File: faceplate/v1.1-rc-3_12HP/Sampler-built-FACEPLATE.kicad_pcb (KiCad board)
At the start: 4 copper layers, 60.6 x 128.5 mm, 24 parts

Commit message: created artwork assets for frontpanel, created and verified gerbers for front panel
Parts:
- removed SD1: microSDCon_Vert_TH_PJS008U-3000, 4ms_Connector_Card:CardSlot_MicroSD_YamaichiPJS008U-3000
- added ?: , , B.Cu at (22.8, 121.3)
- added G***: LOGO, artwork:Sampler-built-frontsilk-v1.1-rc-3_12hp, F.Cu at (23.0, 61.0)
- added REF**: Faceplate_SD_Card_Slot, 4ms_Faceplate:Faceplate_SD_Card_Slot, F.Cu at (22.7, 31.9)
- added REF**: Rail_Connection_12HP, 4ms_Faceplate:Rail_Connection_12HP, B.Cu at (22.8, 1.25)
- moved REF** 9.51 mm to (30.0, 108.7)
- moved REF** 9.51 mm to (30.0, 93.7)
- moved REF** 9.51 mm to (44.5, 93.7)
- moved REF** 9.51 mm to (0.00, 122.5)
- moved REF** 9.51 mm to (0.94, 108.7)
- moved REF** 9.51 mm to (15.5, 93.7)
- moved REF** 9.51 mm to (45.6, 122.5)
- moved REF** 9.51 mm to (0.94, 93.7)
- moved REF** 9.51 mm to (44.5, 108.7)
- moved REF** 9.51 mm to (15.5, 108.7)
- moved LOCK1 9.51 mm to (22.8, 14.4)
- moved REF** 9.51 mm to (41.1, 12.3)
- moved REF** 9.51 mm to (4.13, 27.0)
- moved REF** 9.51 mm to (41.1, 53.0)
- moved REF** 9.51 mm to (4.13, 53.0)
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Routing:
- removed copper zone on In2.Cu, net +3V3
- removed copper zone on In1.Cu, net GND

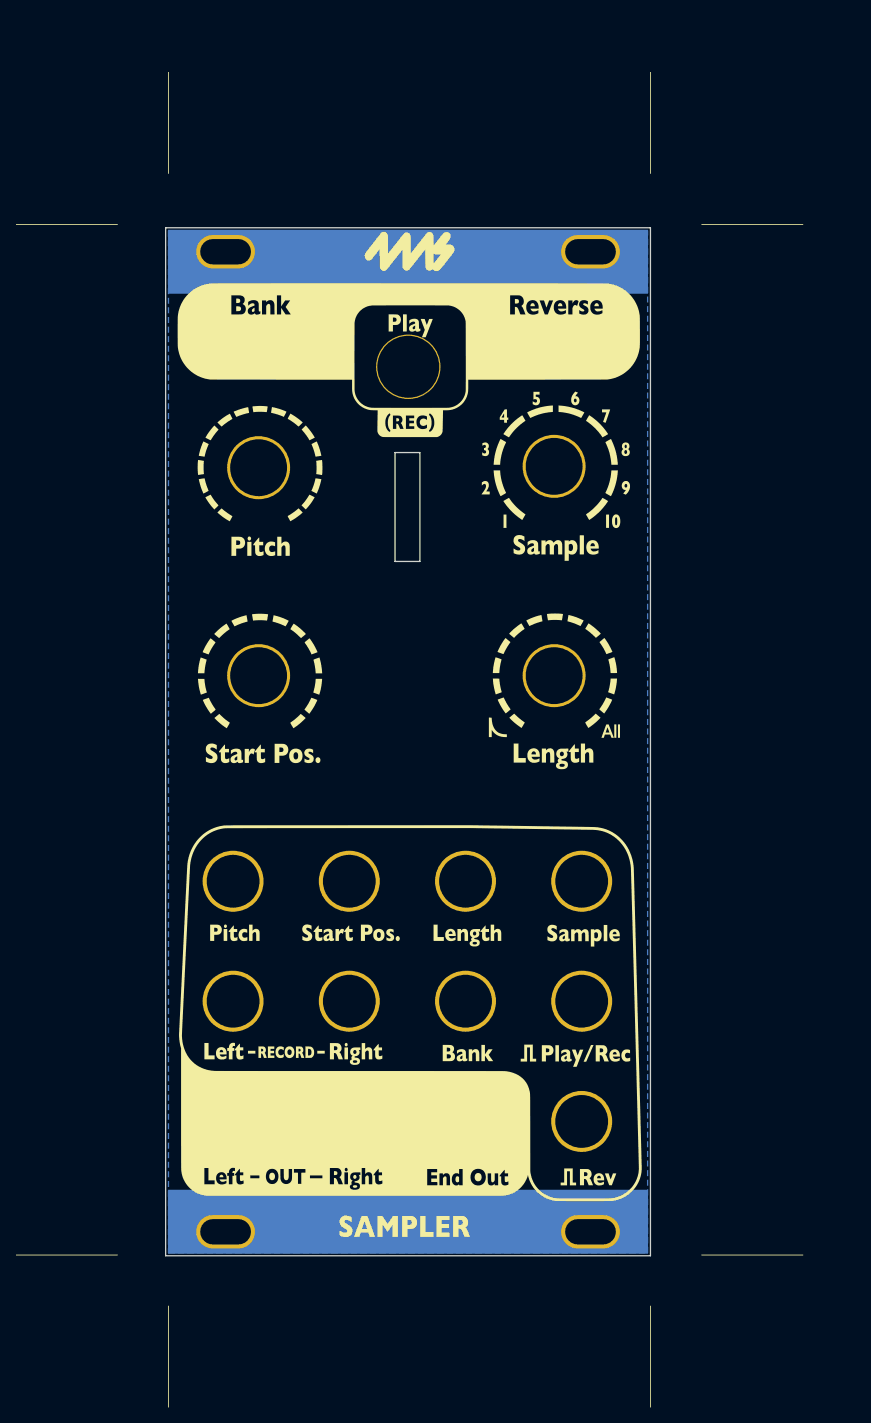
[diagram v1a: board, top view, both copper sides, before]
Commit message: started making new faceplate
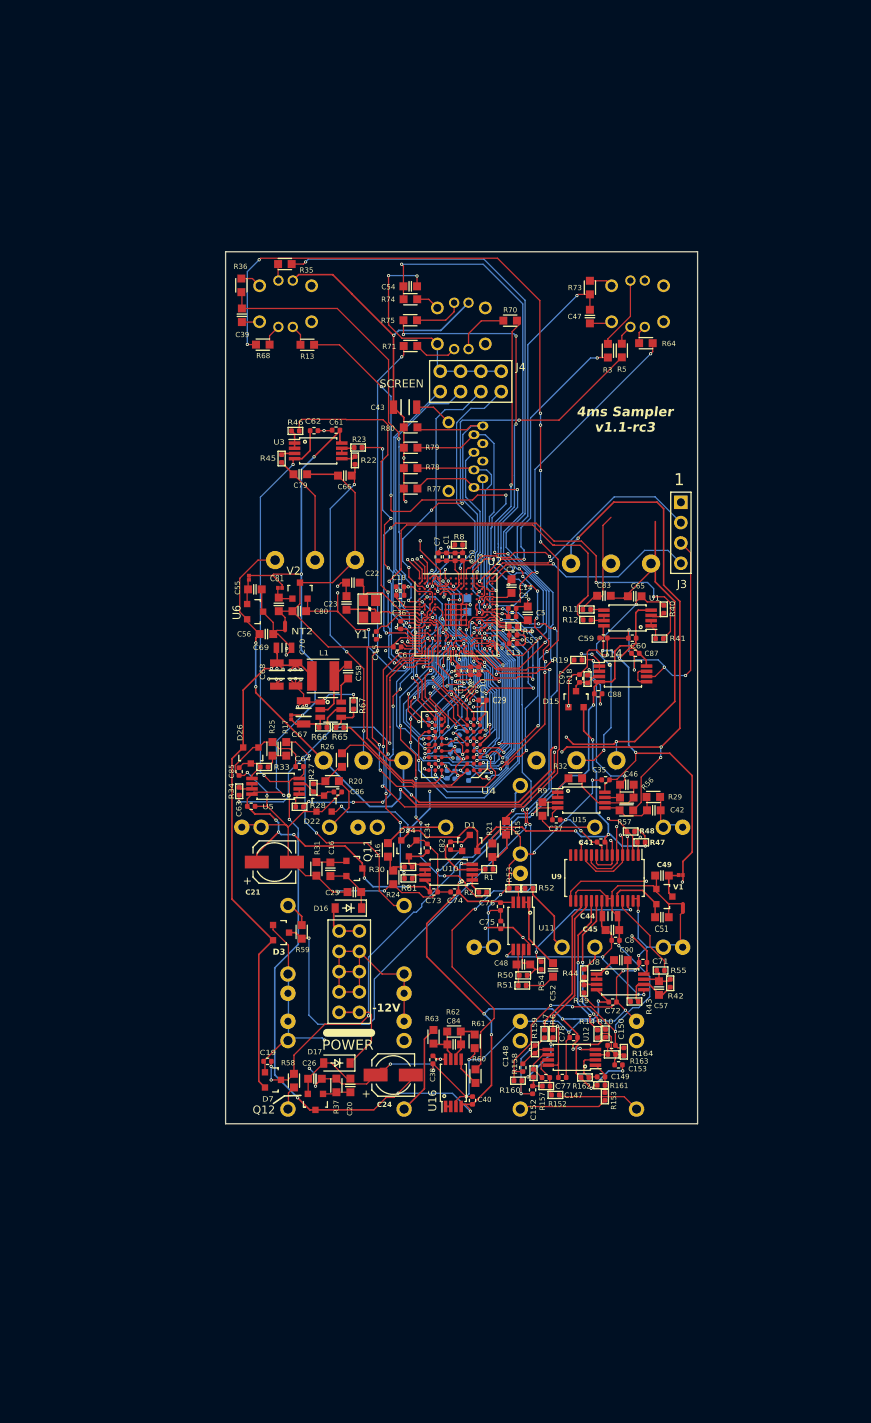
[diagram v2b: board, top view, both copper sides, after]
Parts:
- removed ?: , 
- removed G***: LOGO, artwork:Sampler-built-frontsilk-v1.1-rc-3_12hp
- removed LOCK1: Faceplate_Hole_LED_Button_7mm_With_Mask_Opening, Faceplate_Hole_LED_Button_7mm_With_Mask_Opening
- removed REF** (x2): Faceplate_Hole_LED_Button_5.4mm_With_Mask_Opening, Faceplate_Hole_LED_Button_5.4mm_With_Mask_Opening
- removed REF** (x4): Faceplate_Hole_Pot_16mm, Faceplate_Hole_Pot_16mm
- removed REF** (x12): GND, Faceplate_Hole_Jack_3.5mm
- removed REF** (x4): Faceplate_Rail_Mount_Slot_Plated, Faceplate_Rail_Mount_Slot_Plated
- removed REF**: Faceplate_SD_Card_Slot, 4ms_Faceplate:Faceplate_SD_Card_Slot
- removed REF**: Rail_Connection_12HP, 4ms_Faceplate:Rail_Connection_12HP
- added Bank_But1: Button_SPST_RGB_5.4mmCap, 4ms_Switch:Button_RgbLED_SPST_TC002, B.Cu at (51.5, 6.50)
- added C1: 100nF_0402_16V, 4ms_Capacitor:C_0402, F.Cu at (27.6, 38.1)
- added C10: 100nF_0402_16V, 4ms_Capacitor:C_0402, F.Cu at (31.7, 52.4)
- added C11: 100nF_0402_16V, 4ms_Capacitor:C_0402, F.Cu at (30.6, 52.4)
- added C12: 100nF_0402_16V, 4ms_Capacitor:C_0402, F.Cu at (29.1, 52.4)
- added C13: 100nF_0402_16V, 4ms_Capacitor:C_0402, F.Cu at (35.9, 49.0)
- added C14: 100nF_0402_16V, 4ms_Capacitor:C_0402, F.Cu at (35.8, 44.6)
- added C147: 180pF_0402_25V, 4ms_Capacitor:C_0402, F.Cu at (40.0, 103.2)
- added C148: 180pF_0402_25V, 4ms_Capacitor:C_0402, F.Cu at (37.2, 102.0)
- added C149: 180pF_0402_25V, 4ms_Capacitor:C_0402, F.Cu at (46.9, 103.1)
- added C15: 100nF_0402_16V, 4ms_Capacitor:C_0402, F.Cu at (18.8, 48.0)
- added C150: 180pF_0402_25V, 4ms_Capacitor:C_0402, F.Cu at (48.2, 99.2)
- added C152: 820pF_0402_10v, 4ms_Capacitor:C_0402, F.Cu at (38.4, 104.8)
- added C153: 820pF_0402_10v, 4ms_Capacitor:C_0402, F.Cu at (49.1, 101.6)
- added C16: 100nF_0603_16V, 4ms_Capacitor:C_0603, F.Cu at (13.1, 77.2)
- added C17: 100nF_0402_16V, 4ms_Capacitor:C_0402, F.Cu at (21.8, 42.9)
- added C18: 100nF_0402_16V, 4ms_Capacitor:C_0402, F.Cu at (21.8, 41.9)
- added C19: 10nF_0402_16V, 4ms_Capacitor:C_0402, F.Cu at (5.24, 101.2)
- added C2: 2.2uF_0603_25V, 4ms_Capacitor:C_0603, F.Cu at (35.7, 41.8)
- added C20: 100nF_0603_16V, 4ms_Capacitor:C_0603, F.Cu at (15.6, 104.2)
- added C21: 47uF_5x5.3_16V, 4ms_Capacitor:CP_Elec_5x5.3, F.Cu at (6.10, 76.3)
- added C22: 18pF_0603_50V, 4ms_Capacitor:C_0603, F.Cu at (15.9, 41.4)
- added C23: 18pF_0603_50V, 4ms_Capacitor:C_0603, F.Cu at (15.1, 43.9)
- added C24: 47uF_5x5.3_16V, 4ms_Capacitor:CP_Elec_5x5.3, F.Cu at (21.0, 102.9)
- added C25: 0.1uF_0603_16V, 4ms_Capacitor:C_0603, F.Cu at (16.1, 80.0)
- added C26: 0.1uF_0603_16V, 4ms_Capacitor:C_0603, F.Cu at (11.2, 103.4)
- added C27: 100nF_0402_16V, 4ms_Capacitor:C_0402, B.Cu at (29.6, 60.1)
- added C28: 100nF_0402_16V, 4ms_Capacitor:C_0402, B.Cu at (29.1, 62.8)
- added C29: 100nF_0402_16V, 4ms_Capacitor:C_0402, F.Cu at (32.1, 56.1)
- added C3: 100nF_0402_16V, 4ms_Capacitor:C_0402, F.Cu at (29.6, 38.1)
- added C30: 100nF_0402_16V, 4ms_Capacitor:C_0402, B.Cu at (30.4, 65.6)
- added C31: 100nF_0402_16V, 4ms_Capacitor:C_0402, B.Cu at (27.7, 65.3)
- added C32: 100nF_0402_16V, 4ms_Capacitor:C_0402, B.Cu at (28.7, 65.4)
- added C33: 100nF_0402_16V, 4ms_Capacitor:C_0402, B.Cu at (28.1, 62.1)
- added C34: 10nF_0402_16V, 4ms_Capacitor:C_0402, F.Cu at (25.2, 74.5)
- added C35: 100nF_0402_50V, 4ms_Capacitor:C_0402, F.Cu at (47.5, 66.0)
- added C36: 100nF_0402_16V, 4ms_Capacitor:C_0402, F.Cu at (21.9, 46.7)
- added C37: 100nF_0402_50V, 4ms_Capacitor:C_0402, F.Cu at (41.3, 71.0)
- added C38: 100nF_0402_50V, 4ms_Capacitor:C_0402, F.Cu at (25.9, 101.0)
- added C39: 0.1uF_0603_16V, 4ms_Capacitor:C_0603, F.Cu at (2.04, 7.94)
- added C4: 2.2uF_0603_25V, 4ms_Capacitor:C_0603, B.Cu at (30.2, 44.2)
- added C40: 100nF_0402_50V, 4ms_Capacitor:C_0402, F.Cu at (30.9, 106.1)
- added C41: 100nF_0402_16V, 4ms_Capacitor:C_0402, F.Cu at (46.9, 73.8)
- added C42: 0.1uF_0603_16V, 4ms_Capacitor:C_0603, F.Cu at (53.5, 69.8)
- added C43: 4.7uF_1206_lowESR, 4ms_Capacitor:C_1206, F.Cu at (22.4, 19.4)
- added C44: 22uF_0805_10V, 4ms_Capacitor:C_0805, F.Cu at (48.0, 83.0)
- added C45: 0.1uF_0603_16V, 4ms_Capacitor:C_0603, F.Cu at (48.4, 84.8)
- added C46: 1nF_0603_50V, 4ms_Capacitor:C_0603, F.Cu at (50.2, 66.6)
- added C47: 0.1uF_0603_16V, 4ms_Capacitor:C_0603, F.Cu at (45.5, 8.10)
- added C48: 220pF_0603_25V, 4ms_Capacitor:C_0603, F.Cu at (37.2, 89.1)
- added C49: 2.2uF_0603_25V, 4ms_Capacitor:C_0603, F.Cu at (54.6, 78.0)
- added C5: 2.2uF_0603_25V, 4ms_Capacitor:C_0603, F.Cu at (37.8, 45.2)
- added C50: 100nF_0402_16V, 4ms_Capacitor:C_0402, F.Cu at (28.7, 38.1)
- added C51: 10uF_0603_10V, 4ms_Capacitor:C_0603, F.Cu at (54.5, 83.2)
- added C52: 2.2uF_0603_25V, 4ms_Capacitor:C_0603, F.Cu at (40.9, 89.8)
- added C53: 100nF_0402_16V, 4ms_Capacitor:C_0402, F.Cu at (35.9, 47.9)
- added C54: 0.1uF_0603_16V, 4ms_Capacitor:C_0603, F.Cu at (23.1, 4.32)
- added C55: 2.2uF_0603_25V, 4ms_Capacitor:C_0603, F.Cu at (3.66, 42.2)
- added C56: 10uF_0603_10V, 4ms_Capacitor:C_0603, F.Cu at (5.10, 47.8)
- added C57: 220pF_0603_25V, 4ms_Capacitor:C_0603, F.Cu at (54.2, 92.0)
- added C58: 0.1uF_0603_16V, 4ms_Capacitor:C_0603, F.Cu at (15.3, 52.5)
- added C59: 100nF_0402_50V, 4ms_Capacitor:C_0402, F.Cu at (47.2, 48.3)
- added C6: 100nF_0402_16V, 4ms_Capacitor:C_0402, F.Cu at (21.5, 49.4)
- added C60: 100nF_0402_50V, 4ms_Capacitor:C_0402, F.Cu at (50.8, 48.3)
- added C61: 100nF_0402_50V, 4ms_Capacitor:C_0402, F.Cu at (13.8, 22.3)
- added C62: 100nF_0402_50V, 4ms_Capacitor:C_0402, F.Cu at (11.1, 22.4)
- added C63: 100nF_0402_50V, 4ms_Capacitor:C_0402, F.Cu at (3.19, 69.3)
- added C64: 100nF_0402_50V, 4ms_Capacitor:C_0402, F.Cu at (9.24, 64.4)
- added C65: 0.1uF_0603_16V, 4ms_Capacitor:C_0603, F.Cu at (51.1, 43.1)
- added C66: 0.1uF_0603_16V, 4ms_Capacitor:C_0603, F.Cu at (14.9, 28.0)
- added C67: 22uF_1206_25V, 4ms_Capacitor:C_1206, F.Cu at (9.75, 57.6)
- added C68: 22uF_1206_25V, 4ms_Capacitor:C_1206, F.Cu at (6.41, 52.9)
- added C69: 10uF_0805_25V, 4ms_Capacitor:C_0805, F.Cu at (7.30, 49.5)
- added C7: 100nF_0402_16V, 4ms_Capacitor:C_0402, F.Cu at (26.6, 38.1)
- added C70: 22uF_1206_25V, 4ms_Capacitor:C_1206, F.Cu at (8.74, 52.8)
- added C71: 100nF_0402_50V, 4ms_Capacitor:C_0402, F.Cu at (52.2, 88.8)
- added C72: 100nF_0402_50V, 4ms_Capacitor:C_0402, F.Cu at (48.4, 93.8)
- added C73: 100nF_0402_50V, 4ms_Capacitor:C_0402, F.Cu at (26.0, 80.0)
- added C74: 100nF_0402_50V, 4ms_Capacitor:C_0402, F.Cu at (28.6, 80.0)
- added C75: 100nF_0402_50V, 4ms_Capacitor:C_0402, F.Cu at (34.4, 84.1)
- added C76: 100nF_0402_50V, 4ms_Capacitor:C_0402, F.Cu at (34.4, 81.8)
- added C77: 100nF_0402_50V, 4ms_Capacitor:C_0402, F.Cu at (42.1, 103.2)
- added C78: 100nF_0402_50V, 4ms_Capacitor:C_0402, F.Cu at (43.5, 98.2)
- added C79: 0.1uF_0603_16V, 4ms_Capacitor:C_0603, F.Cu at (9.34, 27.8)
- added C8: 100nF_0402_50V, 4ms_Capacitor:C_0402, F.Cu at (48.8, 86.1)
- added C80: 10uF_0603_10V, 4ms_Capacitor:C_0603, F.Cu at (9.21, 44.9)
- added C81: 2.2uF_0603_25V, 4ms_Capacitor:C_0603, F.Cu at (6.65, 44.1)
- added C82: 10nF_0402_16V, 4ms_Capacitor:C_0402, F.Cu at (28.1, 74.2)
- added C83: 0.1uF_0603_16V, 4ms_Capacitor:C_0603, F.Cu at (47.3, 43.0)
- added C84: 100pF_0603_50V, 4ms_Capacitor:C_0603, F.Cu at (28.6, 99.1)
- added C85: 10nF_0402_16V, 4ms_Capacitor:C_0402, F.Cu at (1.69, 65.0)
- added C86: 10nF_0402_16V, 4ms_Capacitor:C_0402, F.Cu at (14.0, 67.5)
- added C87: 100nF_0402_50V, 4ms_Capacitor:C_0402, F.Cu at (51.2, 50.2)
- added C88: 100nF_0402_50V, 4ms_Capacitor:C_0402, F.Cu at (46.6, 55.2)
- added C9: 100nF_0402_16V, 4ms_Capacitor:C_0402, F.Cu at (35.8, 45.6)
- added C90: 2.2uF_0603_25V, 4ms_Capacitor:C_0603, F.Cu at (49.4, 88.5)
- added C97: 10nF_0402_16V, 4ms_Capacitor:C_0402, F.Cu at (44.2, 53.3)
- added D1: BAT54S, 4ms_Package_SOT:SOT23-3_PO132, F.Cu at (30.5, 73.9)
- added D15: BAT54S, 4ms_Package_SOT:SOT23-3_PO132, F.Cu at (43.8, 55.9)
- added D16: B140HW-7, 4ms_Diode:D_SOD-123, F.Cu at (15.3, 82.0)
- added D17: B140HW-7, 4ms_Diode:D_SOD-123, F.Cu at (13.9, 101.4)
- added D22: BAT54S, 4ms_Package_SOT:SOT23-3_PO132, F.Cu at (12.3, 69.0)
- added D24: BAT54S, 4ms_Package_SOT:SOT23-3_PO132, F.Cu at (22.9, 74.6)
- added D26: BAT54S, 4ms_Package_SOT:SOT23-3_PO132, F.Cu at (3.15, 63.0)
- added D3: BAT54S, 4ms_Package_SOT:SOT23-3_PO132, F.Cu at (6.94, 85.1)
- added D7: BAT54S, 4ms_Package_SOT:SOT23-3_PO132, F.Cu at (5.93, 103.5)
- added J10: Eurorack_Power_10pin_Unshrouded, 4ms_Connector:Pins_2x05_2.54mm_TH_EurorackPower, F.Cu at (15.5, 90.0)
- added J11: 3.5mm_Mono_Switched, 4ms_Jack:EighthInch_PJ398SM, B.Cu at (7.79, 102.0)
- added J12: 3.5mm_Mono_Switched, 4ms_Jack:EighthInch_PJ398SM, B.Cu at (7.79, 86.9)
- added J13: 3.5mm_Mono_Switched, 4ms_Jack:EighthInch_PJ398SM, B.Cu at (51.4, 86.9)
- added J14: 3.5mm_Mono_Switched, 4ms_Jack:EighthInch_PJ398SM, B.Cu at (36.8, 86.9)
- added J15: 3.5mm_Mono_Switched, 4ms_Jack:EighthInch_PJ398SM, B.Cu at (22.3, 102.0)
- added J16: 3.5mm_Mono_Switched, 4ms_Jack:EighthInch_PJ398SM, B.Cu at (51.4, 102.0)
- added J17: 3.5mm_Mono_Switched, 4ms_Jack:EighthInch_PJ398SM, B.Cu at (36.8, 102.0)
- added J2: 3.5mm_Mono_Switched, 4ms_Jack:EighthInch_PJ398SM, B.Cu at (36.8, 71.9)
- added J3: Conn_01x04, 4ms_Connector:Pins_1x04_2.54mm_TH_SWD, F.Cu at (56.9, 35.1)
- added J4: Conn_02x04, 4ms_Connector:Pins_2x04_2.54mm_TH, F.Cu at (30.6, 16.2)
- added J6: 3.5mm_Mono_Switched, 4ms_Jack:EighthInch_PJ398SM, B.Cu at (22.3, 71.9)
- added J7: 3.5mm_Mono_Switched, 4ms_Jack:EighthInch_PJ398SM, B.Cu at (7.79, 71.9)
- added J8: 3.5mm_Mono_Switched, 4ms_Jack:EighthInch_PJ398SM, B.Cu at (51.4, 71.9)
- added J9: 3.5mm_Mono_Switched, 4ms_Jack:EighthInch_PJ398SM, B.Cu at (22.3, 86.9)
- added JP11: JumpForCrystal, 4ms_SolderJumper:JUMPER_SMD_1x2_tiny_shorted, F.Cu at (2.92, 40.7)
- added JP2: JumpForCrystal, 4ms_SolderJumper:JUMPER_SMD_1x2_tiny_shorted, F.Cu at (8.19, 58.2)
- added JP3: JumpForCrystal, 4ms_SolderJumper:JUMPER_SMD_1x2_tiny_shorted, F.Cu at (6.80, 42.0)
- added JP4: JumpForCrystal, 4ms_SolderJumper:JUMPER_SMD_1x2_tiny_shorted, F.Cu at (56.9, 77.9)
- added L1: 4.7uH_1.2A_40xx, Inductor_SMD:L_Taiyo-Yuden_NR-40xx, F.Cu at (12.2, 53.0)
- added NT1: NetTie_2, NetTie:NetTie-2_SMD_Pad0.5mm, F.Cu at (57.2, 82.0)
- added NT2: NetTie_2, NetTie:NetTie-2_SMD_Pad0.5mm, F.Cu at (7.43, 46.8)
- added PLAY_BUT1: Button_SPST_RGB_7mmCap, 4ms_Switch:Button_RgbLED_SPST_PB615303HL-7mm, B.Cu at (29.5, 9.27)
- added POT_LENGTH1: 16mm_NoDet_10k, 4ms_Potentiometer:Pot_16mm_NoDet_RV16AF-4A, B.Cu at (17.2, 50.6)
- added POT_PITCH1: 16mm_CtrDet_10k, 4ms_Potentiometer:Pot_16mm_CtrDet_RV16AF-4A, B.Cu at (48.2, 26.0)
- added POT_SAMP1: 16mm_NoDet_10k, 4ms_Potentiometer:Pot_16mm_NoDet_RV16AF-4A, B.Cu at (11.2, 25.6)
- added POT_START1: 16mm_NoDet_10k, 4ms_Potentiometer:Pot_16mm_NoDet_RV16AF-4A, B.Cu at (43.9, 50.6)
- added Q11: Si2347, 4ms_Package_SOT:SOT23-3_PO132, F.Cu at (16.1, 77.1)
- added Q12: Si2318, 4ms_Package_SOT:SOT23-3_PO132, F.Cu at (11.2, 106.3)
- added R1: 10k_0402, 4ms_Resistor:R_0402, F.Cu at (32.9, 77.2)
- added R10: 10k_0402, 4ms_Resistor:R_0402, F.Cu at (47.5, 97.7)
- added R11: 10k_0402, 4ms_Resistor:R_0402, F.Cu at (45.1, 44.7)
- added R12: 68Ω_0402, 4ms_Resistor:R_0402, F.Cu at (45.2, 46.0)
- added R13: 2k_0603, 4ms_Resistor:R_0603, F.Cu at (10.2, 11.6)
- added R14: 10k_0402, 4ms_Resistor:R_0402, F.Cu at (46.5, 97.8)
- added R15: 47k_0603, 4ms_Resistor:R_0603, F.Cu at (35.1, 72.0)
- added R152: 1k_0402, 4ms_Resistor:R_0402, F.Cu at (41.2, 105.4)
- added R153: 1k_0402, 4ms_Resistor:R_0402, F.Cu at (47.4, 105.6)
- added R157: 24k_0402, 4ms_Resistor:R_0402, F.Cu at (40.1, 104.3)
- added R158: 10k_0402, 4ms_Resistor:R_0402, F.Cu at (38.5, 102.7)
- added R159: 10k_0402, 4ms_Resistor:R_0402, F.Cu at (38.7, 99.7)
- added R16: 47k_0603, 4ms_Resistor:R_0603, F.Cu at (20.3, 74.8)
- added R160: 24k_0402, 4ms_Resistor:R_0402, F.Cu at (36.5, 103.6)
- added R161: 24k_0402, 4ms_Resistor:R_0402, F.Cu at (46.9, 104.2)
- added R162: 10k_0402, 4ms_Resistor:R_0402, F.Cu at (44.9, 103.2)
- added R163: 10k_0402, 4ms_Resistor:R_0402, F.Cu at (48.3, 100.3)
- added R164: 24k_0402, 4ms_Resistor:R_0402, F.Cu at (49.8, 100.0)
- added R17: 47k_0603, 4ms_Resistor:R_0603, F.Cu at (7.58, 62.1)
- added R18: 10k_0402, 4ms_Resistor:R_0402, F.Cu at (45.2, 53.4)
- added R19: 68Ω_0402, 4ms_Resistor:R_0402, F.Cu at (44.1, 51.0)
- added R2: 68Ω_0402, 4ms_Resistor:R_0402, F.Cu at (32.1, 80.1)
- added R20: 47k_0603, 4ms_Resistor:R_0603, F.Cu at (13.3, 66.2)
- added R21: 100k_0603, 4ms_Resistor:R_0603, F.Cu at (33.3, 74.8)
- added R22: 10k_0402, 4ms_Resistor:R_0402, F.Cu at (16.2, 26.1)
- added R23: 68Ω_0402, 4ms_Resistor:R_0402, F.Cu at (16.6, 24.5)
- added R24: 100k_0603, 4ms_Resistor:R_0603, F.Cu at (21.0, 78.2)
- added R25: 100k_0603, 4ms_Resistor:R_0603, F.Cu at (5.86, 62.1)
- added R26: 100k_0603, 4ms_Resistor:R_0603, F.Cu at (14.6, 63.5)
- added R27: 10k_0402, 4ms_Resistor:R_0402, F.Cu at (11.0, 67.0)
- added R28: 68Ω_0402, 4ms_Resistor:R_0402, F.Cu at (9.24, 69.4)
- added R29: 20k_0603, 4ms_Resistor:R_0603, F.Cu at (53.5, 68.2)
- added R3: 2k_0603, 4ms_Resistor:R_0603, F.Cu at (47.8, 12.4)
- added R30: 10k_0402, 4ms_Resistor:R_0402, F.Cu at (22.8, 76.9)
- added R31: 1M_0603, 4ms_Resistor:R_0603, F.Cu at (11.3, 77.1)
- added R32: 100k_0603, 4ms_Resistor:R_0603, F.Cu at (43.7, 65.8)
- added R33: 10k_0402, 4ms_Resistor:R_0402, F.Cu at (4.82, 64.4)
- added R34: 68Ω_0402, 4ms_Resistor:R_0402, F.Cu at (1.70, 67.4)
- added R35: 2k_0603, 4ms_Resistor:R_0603, F.Cu at (7.41, 1.54)
- added R36: 10k_0603, 4ms_Resistor:R_0603, F.Cu at (1.97, 4.20)
- added R37: 1M_0603, 4ms_Resistor:R_0603, F.Cu at (13.8, 104.2)
- added R4: 3k_0402, 4ms_Resistor:R_0402, F.Cu at (36.0, 46.8)
- added R40: 10k_0402, 4ms_Resistor:R_0402, F.Cu at (54.8, 44.7)
- added R41: 68Ω_0402, 4ms_Resistor:R_0402, F.Cu at (54.2, 48.4)
- added R42: 14k_0402, 4ms_Resistor:R_0402, F.Cu at (55.6, 91.4)
- added R43: 100k_0402, 4ms_Resistor:R_0402, F.Cu at (51.1, 93.7)
- added R44: 1k_0402, 4ms_Resistor:R_0402, F.Cu at (44.8, 90.2)
- added R45: 10k_0402, 4ms_Resistor:R_0402, F.Cu at (7.01, 25.9)
- added R46: 68Ω_0402, 4ms_Resistor:R_0402, F.Cu at (8.73, 22.4)
- added R47: 4.7k_0402, 4ms_Resistor:R_0402, F.Cu at (52.0, 73.8)
- added R48: 4.7k_0402, 4ms_Resistor:R_0402, F.Cu at (50.6, 72.5)
- added R49: 1M_0402, 4ms_Resistor:R_0402, F.Cu at (44.8, 92.1)
- added R5: 2k_0603, 4ms_Resistor:R_0603, F.Cu at (49.5, 12.3)
- added R50: 14k_0402, 4ms_Resistor:R_0402, F.Cu at (37.2, 90.4)
- added R51: 100k_0402, 4ms_Resistor:R_0402, F.Cu at (37.1, 91.7)
- added R52: 1k_0402, 4ms_Resistor:R_0402, F.Cu at (37.9, 79.6)
- added R53: 1M_0402, 4ms_Resistor:R_0402, F.Cu at (36.0, 79.6)
- added R54: 1k_0402, 4ms_Resistor:R_0402, F.Cu at (39.4, 89.2)
- added R55: 1k_0402, 4ms_Resistor:R_0402, F.Cu at (54.4, 89.8)
- added R56: 33k_0603, 4ms_Resistor:R_0603, F.Cu at (50.1, 68.2)
- added R57: 33k_0603, 4ms_Resistor:R_0603, F.Cu at (50.1, 69.8)
- added R58: 47k_0603, 4ms_Resistor:R_0603, F.Cu at (8.55, 103.6)
- added R59: 47k_0603, 4ms_Resistor:R_0603, F.Cu at (9.52, 85.0)
- added R6: 10k_0402, 4ms_Resistor:R_0402, F.Cu at (40.9, 97.7)
- added R60: 10k_0603, 4ms_Resistor:R_0603, F.Cu at (31.2, 103.0)
- added R61: 33k_0603, 4ms_Resistor:R_0603, F.Cu at (31.1, 98.7)
- added R62: 47k_0603, 4ms_Resistor:R_0603, F.Cu at (28.6, 97.5)
- added R63: 1k_0603, 4ms_Resistor:R_0603, F.Cu at (26.0, 98.1)
- added R64: 2k_0603, 4ms_Resistor:R_0603, F.Cu at (52.5, 11.4)
- added R65: 31.6k_0402, 4ms_Resistor:R_0402, F.Cu at (14.3, 59.5)
- added R66: 100k_0402, 4ms_Resistor:R_0402, F.Cu at (12.2, 59.5)
- added R67: 10.2k_0402, 4ms_Resistor:R_0402, F.Cu at (16.0, 56.7)
- added R68: 2k_0603, 4ms_Resistor:R_0603, F.Cu at (4.65, 11.6)
- added R7: 10k_0402, 4ms_Resistor:R_0402, F.Cu at (39.9, 97.8)
- added R70: 330Ω_0603, 4ms_Resistor:R_0603, F.Cu at (35.6, 8.61)
- added R71: 330Ω_0603, 4ms_Resistor:R_0603, F.Cu at (23.1, 11.8)
- added R73: 10k_0603, 4ms_Resistor:R_0603, F.Cu at (45.5, 4.48)
- added R74: 10k_0603, 4ms_Resistor:R_0603, F.Cu at (23.1, 5.94)
- added R75: 330Ω_0603, 4ms_Resistor:R_0603, F.Cu at (23.1, 8.56)
- added R77: 33k_0603, 4ms_Resistor:R_0603, F.Cu at (23.1, 29.6)
- added R78: 33k_0603, 4ms_Resistor:R_0603, F.Cu at (23.1, 27.0)
- added R79: 33k_0603, 4ms_Resistor:R_0603, F.Cu at (23.1, 24.5)
- added R8: 10k_0402, 4ms_Resistor:R_0402, F.Cu at (29.1, 36.6)
- added R80: 33k_0603, 4ms_Resistor:R_0603, F.Cu at (23.1, 21.9)
- added R81: 68Ω_0402, 4ms_Resistor:R_0402, F.Cu at (22.9, 78.3)
- added R9: 1k_0603, 4ms_Resistor:R_0603, F.Cu at (39.6, 69.7)
- added REV_BUT1: Button_SPST_RGB_5.4mmCap, 4ms_Switch:Button_RgbLED_SPST_TC002, B.Cu at (7.50, 6.50)
- added SD1: microSDCon_Vert_TH_PJS008U-3000, 4ms_Connector_Card:CardSlot_MicroSD_YamaichiPJS008U-3000, B.Cu at (29.4, 26.0)
- added U1: TL072H, 4ms_Package_SSOP:TSSOP-8_4.4x3mm_Pitch0.65mm, F.Cu at (50.2, 45.8)
- added U10: TL072H, 4ms_Package_SSOP:TSSOP-8_4.4x3mm_Pitch0.65mm, F.Cu at (27.9, 77.6)
- added U11: TL072H, 4ms_Package_SSOP:TSSOP-8_4.4x3mm_Pitch0.65mm, F.Cu at (36.9, 84.3)
- added U12: TL072H, 4ms_Package_SSOP:TSSOP-8_4.4x3mm_Pitch0.65mm, F.Cu at (43.3, 100.7)
- added U13: AP62200WU-7, 4ms_Package_SOT:TSOT-23-6, F.Cu at (13.1, 57.2)
- added U14: TL072H, 4ms_Package_SSOP:TSSOP-8_4.4x3mm_Pitch0.65mm, F.Cu at (49.7, 52.8)
- added U15: TL072H, 4ms_Package_SSOP:TSSOP-8_4.4x3mm_Pitch0.65mm, F.Cu at (44.5, 68.5)
- added U16: TL072H, 4ms_Package_SSOP:TSSOP-8_4.4x3mm_Pitch0.65mm, F.Cu at (28.5, 103.9)
- added U2: STM32F746IE, Package_BGA:UFBGA-201_10x10mm_Layout15x15_P0.65mm, F.Cu at (28.8, 45.4)
- added U3: TL072H, 4ms_Package_SSOP:TSSOP-8_4.4x3mm_Pitch0.65mm, F.Cu at (11.6, 24.9)
- added U4: SDRAM_IS42S16400J-6BLI-TR, 4ms_Package_QFP:BGA-54_8.0x8.0mm_P0.8, F.Cu at (28.6, 61.6)
- added U5: TL072H, 4ms_Package_SSOP:TSSOP-8_4.4x3mm_Pitch0.65mm, F.Cu at (6.25, 66.8)
- added U6: NCP51460SN33, 4ms_Package_SOT:SOT23-3_PO132, F.Cu at (3.69, 45.0)
- added U8: TL072H, 4ms_Package_SSOP:TSSOP-8_4.4x3mm_Pitch0.65mm, F.Cu at (49.3, 91.3)
- added U9: PCM3060PW, Package_SO:TSSOP-28_4.4x9.7mm_P0.65mm, F.Cu at (47.4, 78.3)
- added V1: AP2120N-5.0TRG1, 4ms_Package_SOT:SOT23-3_PO132, F.Cu at (54.9, 80.6)
- added V2: AP7384-33, 4ms_Package_SOT:SOT23-3_PO132, F.Cu at (9.30, 42.4)
- added Y1: 16MHz_18pF_FA238, 4ms_Crystal:FA-238, F.Cu at (18.0, 44.6)
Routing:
- net GND: track 0.00 -> 536.3 mm, vias 0 -> 68
- net +3V3: track 0.00 -> 386.9 mm, vias 0 -> 29
- net +12V: track 0.00 -> 251.4 mm, vias 0 -> 18
- net -12VA: track 0.00 -> 250.2 mm, vias 0 -> 16
- net VREF+: track 0.00 -> 167.9 mm, vias 0 -> 10
- net GNDADC: track 0.00 -> 146.2 mm, vias 0 -> 4
- net /D7: track 0.00 -> 124.0 mm, vias 0 -> 10
- net /D8: track 0.00 -> 88.1 mm, vias 0 -> 6
- net /D2: track 0.00 -> 87.9 mm, vias 0 -> 6
- net /D10: track 0.00 -> 87.8 mm, vias 0 -> 2
- net /D13: track 0.00 -> 84.1 mm, vias 0 -> 4
- net /SAI_FS: track 0.00 -> 78.2 mm, vias 0 -> 2
- net /D15: track 0.00 -> 77.0 mm, vias 0 -> 6
- net /SAI_SCK: track 0.00 -> 75.0 mm, vias 0 -> 2
- net /CODEC_RESET: track 0.00 -> 74.1 mm, vias 0 -> 2
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- added copper zone on In2.Cu, net +3V3
- added copper zone on In1.Cu, net GND
- removed copper zone on B.Cu, net GND
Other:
- board size 60.6 x 128.5 mm -> 59 x 109 mm
- board text added: "4ms Sampler v1.1-rc3"
- board text added: "SCREEN"

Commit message: created faceplate
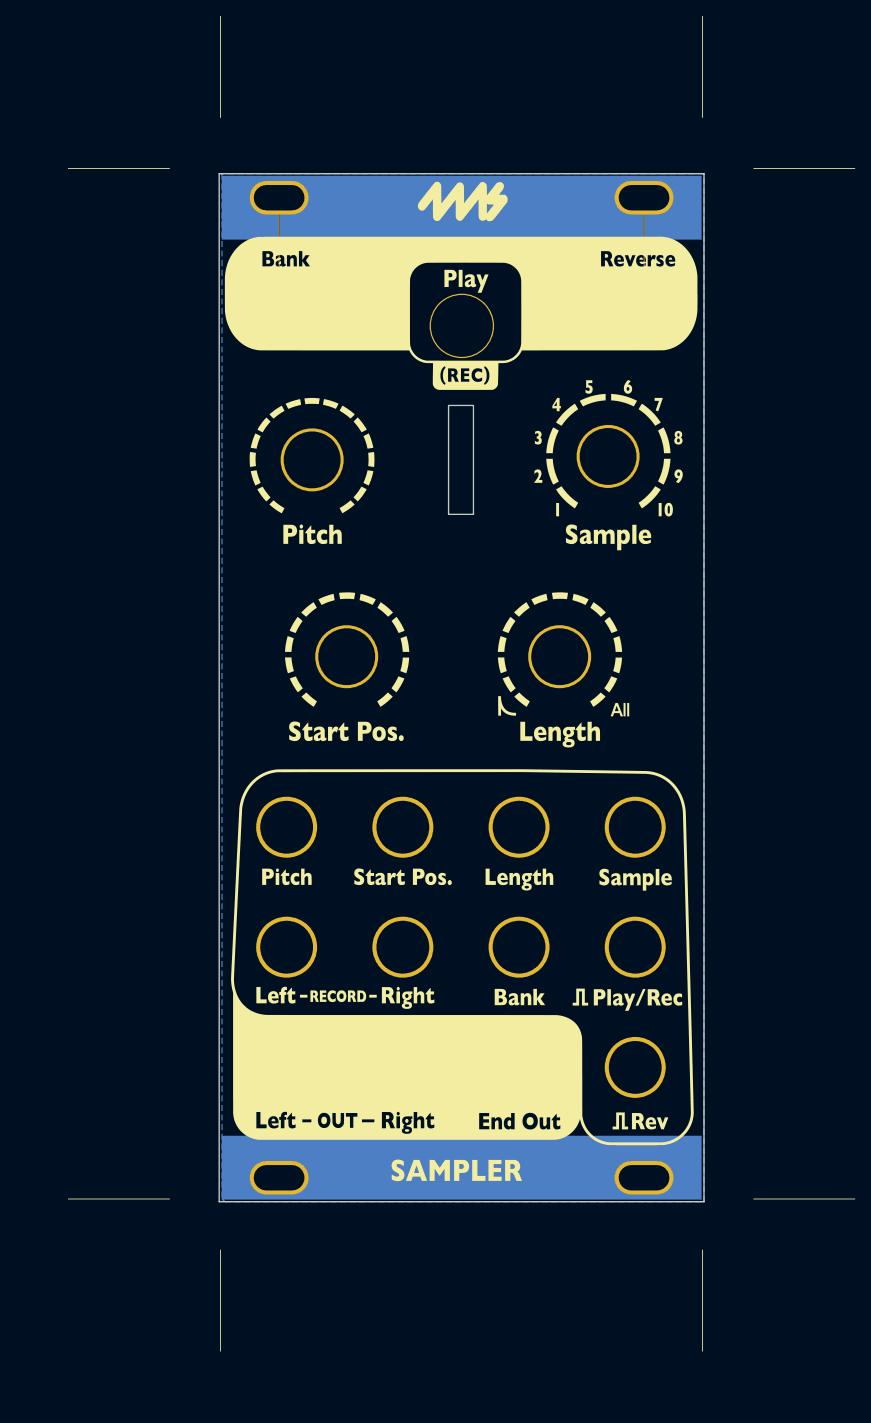
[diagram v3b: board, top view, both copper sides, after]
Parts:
- removed Bank_But1, REV_BUT1: Button_SPST_RGB_5.4mmCap, 4ms_Switch:Button_RgbLED_SPST_TC002
- removed C1, C10, C11, C12, C13, C14, C15, C17, C18, C27, C28, C29, C3, C30, C31, C32, C33, C36, C41, C50, C53, C6, C7, C9: 100nF_0402_16V, 4ms_Capacitor:C_0402
- removed C147, C148, C149, C150: 180pF_0402_25V, 4ms_Capacitor:C_0402
- removed C152, C153: 820pF_0402_10v, 4ms_Capacitor:C_0402
- removed C16, C20: 100nF_0603_16V, 4ms_Capacitor:C_0603
- removed C19, C34, C82, C85, C86, C97: 10nF_0402_16V, 4ms_Capacitor:C_0402
- removed C2, C4, C49, C5, C52, C55, C81, C90: 2.2uF_0603_25V, 4ms_Capacitor:C_0603
- removed C21, C24: 47uF_5x5.3_16V, 4ms_Capacitor:CP_Elec_5x5.3
- removed C22, C23: 18pF_0603_50V, 4ms_Capacitor:C_0603
- removed C25, C26, C39, C42, C45, C47, C54, C58, C65, C66, C79, C83: 0.1uF_0603_16V, 4ms_Capacitor:C_0603
- removed C35, C37, C38, C40, C59, C60, C61, C62, C63, C64, C71, C72, C73, C74, C75, C76, C77, C78, C8, C87, C88: 100nF_0402_50V, 4ms_Capacitor:C_0402
- removed C43: 4.7uF_1206_lowESR, 4ms_Capacitor:C_1206
- removed C44: 22uF_0805_10V, 4ms_Capacitor:C_0805
- removed C46: 1nF_0603_50V, 4ms_Capacitor:C_0603
- removed C48, C57: 220pF_0603_25V, 4ms_Capacitor:C_0603
- removed C51, C56, C80: 10uF_0603_10V, 4ms_Capacitor:C_0603
- removed C67, C68, C70: 22uF_1206_25V, 4ms_Capacitor:C_1206
- removed C69: 10uF_0805_25V, 4ms_Capacitor:C_0805
- removed C84: 100pF_0603_50V, 4ms_Capacitor:C_0603
- removed D1, D15, D22, D24, D26, D3, D7: BAT54S, 4ms_Package_SOT:SOT23-3_PO132
- removed D16, D17: B140HW-7, 4ms_Diode:D_SOD-123
- removed J10: Eurorack_Power_10pin_Unshrouded, 4ms_Connector:Pins_2x05_2.54mm_TH_EurorackPower
- removed J11, J12, J13, J14, J15, J16, J17, J2, J6, J7, J8, J9: 3.5mm_Mono_Switched, 4ms_Jack:EighthInch_PJ398SM
- removed J3: Conn_01x04, 4ms_Connector:Pins_1x04_2.54mm_TH_SWD
- removed J4: Conn_02x04, 4ms_Connector:Pins_2x04_2.54mm_TH
- removed JP11, JP2, JP3, JP4: JumpForCrystal, 4ms_SolderJumper:JUMPER_SMD_1x2_tiny_shorted
- removed L1: 4.7uH_1.2A_40xx, Inductor_SMD:L_Taiyo-Yuden_NR-40xx
- removed NT1, NT2: NetTie_2, NetTie:NetTie-2_SMD_Pad0.5mm
- removed PLAY_BUT1: Button_SPST_RGB_7mmCap, 4ms_Switch:Button_RgbLED_SPST_PB615303HL-7mm
- removed POT_LENGTH1, POT_SAMP1, POT_START1: 16mm_NoDet_10k, 4ms_Potentiometer:Pot_16mm_NoDet_RV16AF-4A
- removed POT_PITCH1: 16mm_CtrDet_10k, 4ms_Potentiometer:Pot_16mm_CtrDet_RV16AF-4A
- removed Q11: Si2347, 4ms_Package_SOT:SOT23-3_PO132
- removed Q12: Si2318, 4ms_Package_SOT:SOT23-3_PO132
- removed R1, R10, R11, R14, R158, R159, R162, R163, R18, R22, R27, R30, R33, R40, R45, R6, R7, R8: 10k_0402, 4ms_Resistor:R_0402
- removed R12, R19, R2, R23, R28, R34, R41, R46, R81: 68Ω_0402, 4ms_Resistor:R_0402
- removed R13, R3, R35, R5, R64, R68: 2k_0603, 4ms_Resistor:R_0603
- removed R15, R16, R17, R20, R58, R59, R62: 47k_0603, 4ms_Resistor:R_0603
- removed R152, R153, R44, R52, R54, R55: 1k_0402, 4ms_Resistor:R_0402
- removed R157, R160, R161, R164: 24k_0402, 4ms_Resistor:R_0402
- removed R21, R24, R25, R26, R32: 100k_0603, 4ms_Resistor:R_0603
- removed R29: 20k_0603, 4ms_Resistor:R_0603
- removed R31, R37: 1M_0603, 4ms_Resistor:R_0603
- removed R36, R60, R73, R74: 10k_0603, 4ms_Resistor:R_0603
- removed R4: 3k_0402, 4ms_Resistor:R_0402
- removed R42, R50: 14k_0402, 4ms_Resistor:R_0402
- removed R43, R51, R66: 100k_0402, 4ms_Resistor:R_0402
- removed R47, R48: 4.7k_0402, 4ms_Resistor:R_0402
- removed R49, R53: 1M_0402, 4ms_Resistor:R_0402
- removed R56, R57, R61, R77, R78, R79, R80: 33k_0603, 4ms_Resistor:R_0603
- removed R63, R9: 1k_0603, 4ms_Resistor:R_0603
- removed R65: 31.6k_0402, 4ms_Resistor:R_0402
- removed R67: 10.2k_0402, 4ms_Resistor:R_0402
- removed R70, R71, R75: 330Ω_0603, 4ms_Resistor:R_0603
- removed SD1: microSDCon_Vert_TH_PJS008U-3000, 4ms_Connector_Card:CardSlot_MicroSD_YamaichiPJS008U-3000
- removed U1, U10, U11, U12, U14, U15, U16, U3, U5, U8: TL072H, 4ms_Package_SSOP:TSSOP-8_4.4x3mm_Pitch0.65mm
- removed U13: AP62200WU-7, 4ms_Package_SOT:TSOT-23-6
- removed U2: STM32F746IE, Package_BGA:UFBGA-201_10x10mm_Layout15x15_P0.65mm
- removed U4: SDRAM_IS42S16400J-6BLI-TR, 4ms_Package_QFP:BGA-54_8.0x8.0mm_P0.8
- removed U6: NCP51460SN33, 4ms_Package_SOT:SOT23-3_PO132
- removed U9: PCM3060PW, Package_SO:TSSOP-28_4.4x9.7mm_P0.65mm
- removed V1: AP2120N-5.0TRG1, 4ms_Package_SOT:SOT23-3_PO132
- removed V2: AP7384-33, 4ms_Package_SOT:SOT23-3_PO132
- removed Y1: 16MHz_18pF_FA238, 4ms_Crystal:FA-238
- added G***: LOGO, artwork:artwork-silkscreen-v1.1-rc3_12hp, F.Cu at (29.5, 54.0)
- added LOCK1: Faceplate_Hole_LED_Button_7mm_With_Mask_Opening, Faceplate_Hole_LED_Button_7mm_With_Mask_Opening, F.Cu at (29.5, 9.27)
- added REF**: Faceplate_Hole_Pot_16mm, Faceplate_Hole_Pot_16mm, F.Cu at (10.8, 26.0)
- added REF**: Faceplate_SD_Card_Slot, 4ms_Faceplate:Faceplate_SD_Card_Slot, F.Cu at (29.4, 26.0)
- added REF**: Faceplate_Rail_Mount_Slot_Plated, Faceplate_Rail_Mount_Slot_Plated, F.Cu at (52.3, 115.8)
- added REF**: GND, Faceplate_Hole_Jack_3.5mm, F.Cu at (51.2, 86.9)
- added REF**: GND, Faceplate_Hole_Jack_3.5mm, F.Cu at (51.2, 102.0)
- added REF**: GND, Faceplate_Hole_Jack_3.5mm, F.Cu at (51.2, 71.9)
- added REF**: Faceplate_Hole_LED_Button_5.4mm_With_Mask_Opening, Faceplate_Hole_LED_Button_5.4mm_With_Mask_Opening, F.Cu at (7.50, 6.50)
- added REF**: Faceplate_Rail_Mount_Slot_Plated, Faceplate_Rail_Mount_Slot_Plated, F.Cu at (6.69, 115.8)
- added REF**: GND, Faceplate_Hole_Jack_3.5mm, F.Cu at (22.2, 71.9)
- added REF**: Faceplate_Hole_Pot_16mm, Faceplate_Hole_Pot_16mm, F.Cu at (41.8, 50.6)
- added REF**: GND, Faceplate_Hole_Jack_3.5mm, F.Cu at (22.2, 86.9)
- added REF**: Faceplate_Hole_Pot_16mm, Faceplate_Hole_Pot_16mm, F.Cu at (15.1, 50.6)
- added REF**: GND, Faceplate_Hole_Jack_3.5mm, F.Cu at (36.7, 71.9)
- added REF**: GND, Faceplate_Hole_Jack_3.5mm, F.Cu at (22.2, 102.0)
- added REF**: Faceplate_Hole_LED_Button_5.4mm_With_Mask_Opening, Faceplate_Hole_LED_Button_5.4mm_With_Mask_Opening, F.Cu at (51.5, 6.50)
- added REF**: Faceplate_Rail_Mount_Slot_Plated, Faceplate_Rail_Mount_Slot_Plated, F.Cu at (6.69, -6.75)
- added REF**: Rail_Connection_12HP, 4ms_Faceplate:Rail_Connection_12HP, B.Cu at (29.5, -5.50)
- added REF**: Rail_Connection_12HP, 4ms_Faceplate:Rail_Connection_12HP, B.Cu at (29.5, 114.6)
- added REF**: GND, Faceplate_Hole_Jack_3.5mm, F.Cu at (7.63, 71.9)
- added REF**: Faceplate_Hole_Pot_16mm, Faceplate_Hole_Pot_16mm, F.Cu at (47.8, 25.6)
- added REF**: GND, Faceplate_Hole_Jack_3.5mm, F.Cu at (36.7, 86.9)
- added REF**: GND, Faceplate_Hole_Jack_3.5mm, F.Cu at (7.63, 102.0)
- added REF**: Faceplate_Rail_Mount_Slot_Plated, Faceplate_Rail_Mount_Slot_Plated, F.Cu at (52.3, -6.75)
- added REF**: GND, Faceplate_Hole_Jack_3.5mm, F.Cu at (7.63, 86.9)
- added REF**: GND, Faceplate_Hole_Jack_3.5mm, F.Cu at (36.7, 102.0)
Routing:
- net GND: track 536.3 -> 27.2 mm, vias 68 -> 0
- net +3V3: track 386.9 -> 0.00 mm, vias 29 -> 0
- net +12V: track 251.4 -> 0.00 mm, vias 18 -> 0
- net -12VA: track 250.2 -> 0.00 mm, vias 16 -> 0
- net VREF+: track 167.9 -> 0.00 mm, vias 10 -> 0
- net GNDADC: track 146.2 -> 0.00 mm, vias 4 -> 0
- net /D7: track 124.0 -> 0.00 mm, vias 10 -> 0
- net /D8: track 88.1 -> 0.00 mm, vias 6 -> 0
- net /D2: track 87.9 -> 0.00 mm, vias 6 -> 0
- net /D10: track 87.8 -> 0.00 mm, vias 2 -> 0
- net /D13: track 84.1 -> 0.00 mm, vias 4 -> 0
- net /SAI_FS: track 78.2 -> 0.00 mm, vias 2 -> 0
- net /D15: track 77.0 -> 0.00 mm, vias 6 -> 0
- net /SAI_SCK: track 75.0 -> 0.00 mm, vias 2 -> 0
- net /CODEC_RESET: track 74.1 -> 0.00 mm, vias 2 -> 0
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- added copper zone on B.Cu, net GND
- removed copper zone on In2.Cu, net +3V3
- removed copper zone on In1.Cu, net GND
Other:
- board size 59 x 109 mm -> 60.6 x 128.5 mm
- board text removed: "4ms Sampler v1.1-rc3"
- board text removed: "SCREEN"
